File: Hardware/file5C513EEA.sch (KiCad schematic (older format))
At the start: 72 parts, among them J10 IN_2, J11 IN_3, J12 PWM_CV, J4 OUT2_CON, J5 EXT_CON, J6 CUTOFF_CV, J7 SHAPE_CV, J8 OUT1_CON, J9 IN_1, U2 MCP6002-xSN, U3 MCP6004, U4 OPA1678, U5 MCP6002-xSN

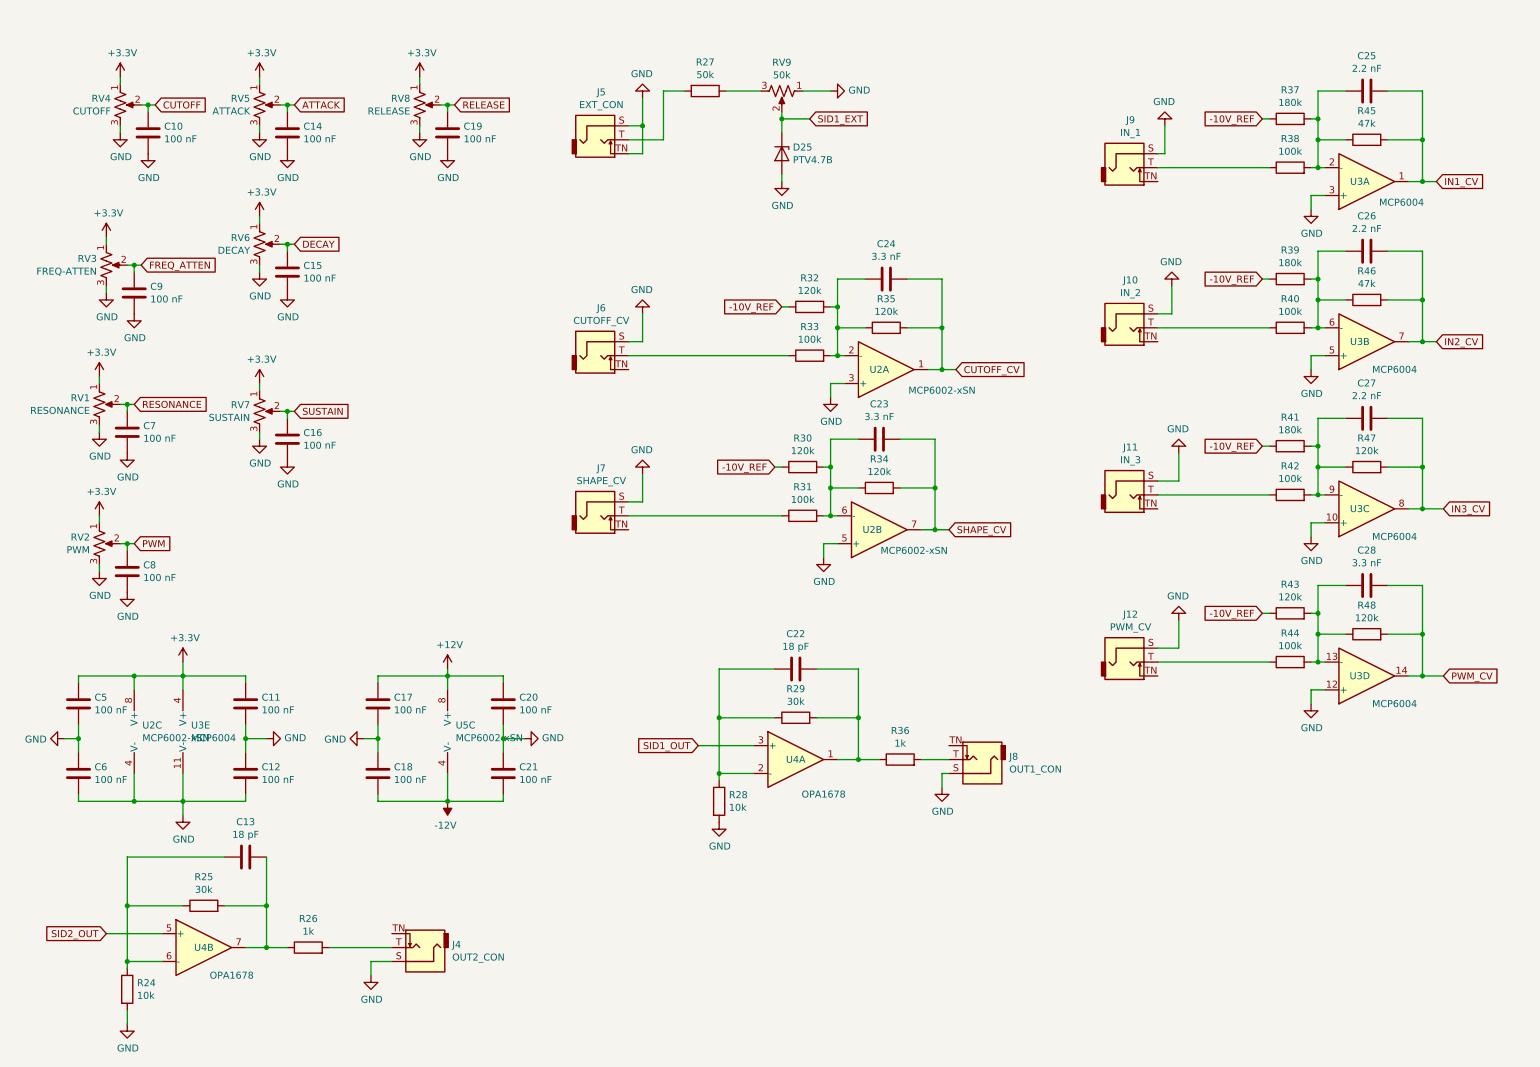
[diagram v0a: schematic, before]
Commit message: Started board layout
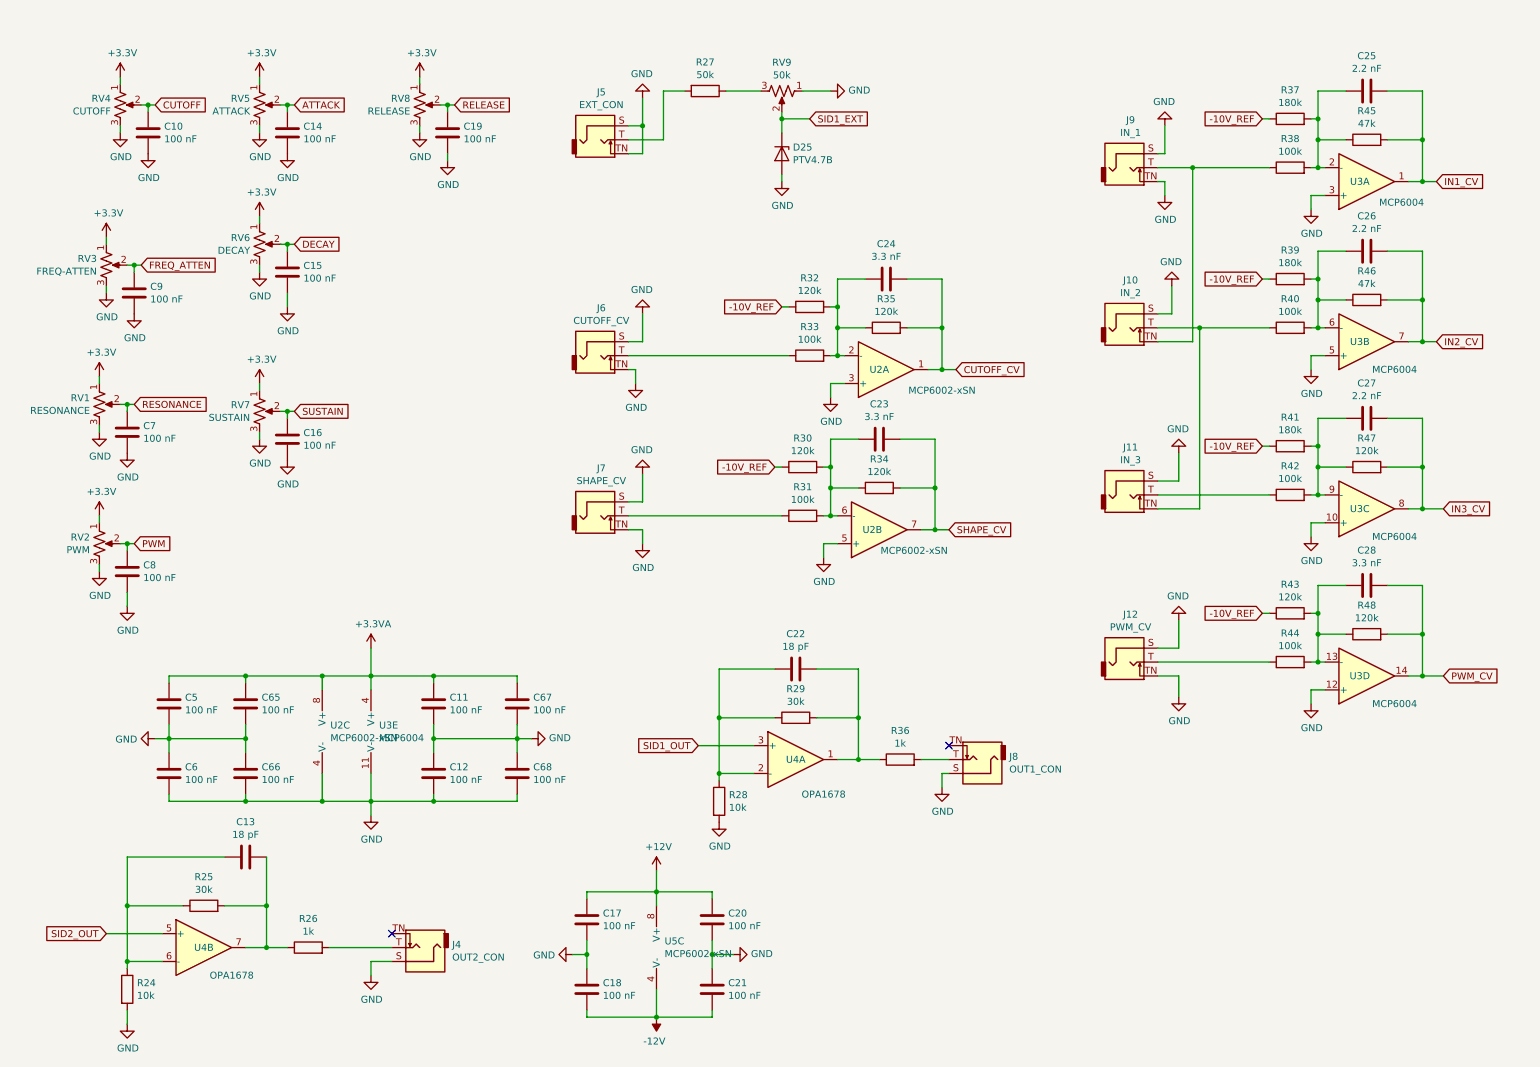
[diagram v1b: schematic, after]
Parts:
- added C65, C66, C67, C68: 100 nF, symbol Device:C
- C10, C11, C12, C13, C14, C15, C16, C17, C18, C19, C20, C21, C22, C23, C24, C25, C26, C27, C28, C5, C6, C7, C8, C9: footprint (none) -> Capacitors_SMD:C_0603
- U2, U4, U5: footprint (none) -> Housings_SOIC:SOIC-8_3.9x4.9mm_Pitch1.27mm
- U3: footprint (none) -> Housings_SSOP:TSSOP-14_4.4x5mm_Pitch0.65mm
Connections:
- net +3V3: no longer C11.1, C5.1, U2.8 (V+), U3.4 (V+)
- net GND: now also J12.TN, J6.TN, J7.TN, J9.TN, C65.2, C66.1, C66.2, C67.2, C68.1, C68.2
- net at J9.T, R38.1: now also J10.TN
- net at J10.T, R40.1: now also J11.TN
- new net +3.3VA: C11.1, C5.1, C65.1, C67.1, U2.8 (V+), U3.4 (V+)
- no-connect marks 0 -> 2
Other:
- moved on the sheet: C11, C12, C17, C18, C20, C21, C5, C6, U2C, U3E, U5C

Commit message: Fixed issues with footprints
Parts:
- C10, C11, C12, C13, C14, C15, C16, C17, C18, C19, C20, C21, C22, C23, C24, C25, C26, C27, C28, C5, C6, C7, C8, C9: footprint Capacitors_SMD:C_0603 -> Capacitor_SMD:C_0603_1608Metric
- C65, C66, C67, C68: footprint (none) -> Capacitor_SMD:C_0603_1608Metric
- U2, U4, U5: footprint Housings_SOIC:SOIC-8_3.9x4.9mm_Pitch1.27mm -> Package_SO:SOIC-8_3.9x4.9mm_P1.27mm
- U3: footprint Housings_SSOP:TSSOP-14_4.4x5mm_Pitch0.65mm -> Package_SO:TSSOP-14_4.4x5mm_P0.65mm

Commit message: Added PJ398SM model
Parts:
- J10, J11, J12, J4, J5, J6, J7, J8, J9: footprint (none) -> Connector_Audio:Jack_3.5mm_QingPu_WQP-PJ398SM_Vertical_CircularHoles
- R24, R25, R26, R27, R28, R29, R30, R31, R32, R33, R34, R35, R36, R37, R38, R39, R40, R41, R42, R43, R44, R45, R46, R47, R48: footprint (none) -> Resistor_SMD:R_0603_1608Metric
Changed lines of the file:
@@
 F 0 "J8" H 7117 5629 50  0000 R CNN
 F 1 "OUT1_CON" H 7117 5720 50  0000 R CNN
-F 2 "" H 7350 5650 50  0001 C CNN
+F 2 "Connector_Audio:Jack_3.5mm_QingPu_WQP-PJ398SM_Vertical_CircularHoles" H 7350 5650 50  0001 C CNN
 F 3 "~" H 7350 5650 50  0001 C CNN
 	1    7350 5650
@@
 F 0 "J4" H 3117 6979 50  0000 R CNN
 F 1 "OUT2_CON" H 3117 7070 50  0000 R CNN
-F 2 "" H 3350 7000 50  0001 C CNN
+F 2 "Connector_Audio:Jack_3.5mm_QingPu_WQP-PJ398SM_Vertical_CircularHoles" H 3350 7000 50  0001 C CNN
 F 3 "~" H 3350 7000 50  0001 C CNN
 	1    3350 7000
@@
 F 0 "R28" H 5570 5996 50  0000 L CNN
 F 1 "10k" H 5570 5905 50  0000 L CNN
-F 2 "" V 5430 5950 50  0001 C CNN
+F 2 "Resistor_SMD:R_0603_1608Metric" V 5430 5950 50  0001 C CNN
 F 3 "~" H 5500 5950 50  0001 C CNN
 	1    5500 5950
@@
 F 0 "R29" V 6257 5350 50  0000 C CNN
 F 1 "30k" V 6166 5350 50  0000 C CNN
-F 2 "" V 5980 5350 50  0001 C CNN
+F 2 "Resistor_SMD:R_0603_1608Metric" V 5980 5350 50  0001 C CNN
 F 3 "~" H 6050 5350 50  0001 C CNN
 	1    6050 5350
@@
 F 0 "R36" V 7007 5650 50  0000 C CNN
 F 1 "1k" V 6916 5650 50  0000 C CNN
-F 2 "" V 6730 5650 50  0001 C CNN
+F 2 "Resistor_SMD:R_0603_1608Metric" V 6730 5650 50  0001 C CNN
 F 3 "~" H 6800 5650 50  0001 C CNN
 	1    6800 5650
@@
 F 0 "R24" H 1320 7346 50  0000 L CNN
 F 1 "10k" H 1320 7255 50  0000 L CNN
-F 2 "" V 1180 7300 50  0001 C CNN
+F 2 "Resistor_SMD:R_0603_1608Metric" V 1180 7300 50  0001 C CNN
 F 3 "~" H 1250 7300 50  0001 C CNN
 	1    1250 7300
@@
 F 0 "R25" V 2007 6700 50  0000 C CNN
 F 1 "30k" V 1916 6700 50  0000 C CNN
-F 2 "" V 1730 6700 50  0001 C CNN
+F 2 "Resistor_SMD:R_0603_1608Metric" V 1730 6700 50  0001 C CNN
 F 3 "~" H 1800 6700 50  0001 C CNN
 	1    1800 6700
@@
 F 0 "R26" V 2757 7000 50  0000 C CNN
 F 1 "1k" V 2666 7000 50  0000 C CNN
-F 2 "" V 2480 7000 50  0001 C CNN
+F 2 "Resistor_SMD:R_0603_1608Metric" V 2480 7000 50  0001 C CNN
 F 3 "~" H 2550 7000 50  0001 C CNN
 	1    2550 7000
@@
 F 0 "J9" H 8454 1742 50  0000 C CNN
 F 1 "IN_1" H 8454 1651 50  0000 C CNN
-F 2 "" H 8450 1400 50  0001 C CNN
+F 2 "Connector_Audio:Jack_3.5mm_QingPu_WQP-PJ398SM_Vertical_CircularHoles" H 8450 1400 50  0001 C CNN
 F 3 "~" H 8450 1400 50  0001 C CNN
 	1    8450 1400
@@
 F 0 "R38" V 9807 1400 50  0000 C CNN
 F 1 "100k" V 9716 1400 50  0000 C CNN
-F 2 "" V 9530 1400 50  0001 C CNN
+F 2 "Resistor_SMD:R_0603_1608Metric" V 9530 1400 50  0001 C CNN
 F 3 "~" H 9600 1400 50  0001 C CNN
 	1    9600 1400
@@
 F 0 "R37" V 9807 1050 50  0000 C CNN
 F 1 "180k" V 9716 1050 50  0000 C CNN
-F 2 "" V 9530 1050 50  0001 C CNN
+F 2 "Resistor_SMD:R_0603_1608Metric" V 9530 1050 50  0001 C CNN
 F 3 "~" H 9600 1050 50  0001 C CNN
 	1    9600 1050
@@
 F 0 "R45" V 10357 1200 50  0000 C CNN
 F 1 "47k" V 10266 1200 50  0000 C CNN
-F 2 "" V 10080 1200 50  0001 C CNN
+F 2 "Resistor_SMD:R_0603_1608Metric" V 10080 1200 50  0001 C CNN
 F 3 "~" H 10150 1200 50  0001 C CNN
 	1    10150 1200
@@
 F 0 "J10" H 8454 2892 50  0000 C CNN
 F 1 "IN_2" H 8454 2801 50  0000 C CNN
-F 2 "" H 8450 2550 50  0001 C CNN
+F 2 "Connector_Audio:Jack_3.5mm_QingPu_WQP-PJ398SM_Vertical_CircularHoles" H 8450 2550 50  0001 C CNN
 F 3 "~" H 8450 2550 50  0001 C CNN
 	1    8450 2550
@@
 F 0 "R40" V 9807 2550 50  0000 C CNN
 F 1 "100k" V 9716 2550 50  0000 C CNN
-F 2 "" V 9530 2550 50  0001 C CNN
+F 2 "Resistor_SMD:R_0603_1608Metric" V 9530 2550 50  0001 C CNN
 F 3 "~" H 9600 2550 50  0001 C CNN
 	1    9600 2550
@@
 F 0 "R39" V 9807 2200 50  0000 C CNN
 F 1 "180k" V 9716 2200 50  0000 C CNN
-F 2 "" V 9530 2200 50  0001 C CNN
+F 2 "Resistor_SMD:R_0603_1608Metric" V 9530 2200 50  0001 C CNN
 F 3 "~" H 9600 2200 50  0001 C CNN
 	1    9600 2200
@@
 F 0 "R46" V 10357 2350 50  0000 C CNN
 F 1 "47k" V 10266 2350 50  0000 C CNN
-F 2 "" V 10080 2350 50  0001 C CNN
+F 2 "Resistor_SMD:R_0603_1608Metric" V 10080 2350 50  0001 C CNN
 F 3 "~" H 10150 2350 50  0001 C CNN
 	1    10150 2350
@@
 F 0 "J11" H 8454 4092 50  0000 C CNN
 F 1 "IN_3" H 8454 4001 50  0000 C CNN
-F 2 "" H 8450 3750 50  0001 C CNN
+F 2 "Connector_Audio:Jack_3.5mm_QingPu_WQP-PJ398SM_Vertical_CircularHoles" H 8450 3750 50  0001 C CNN
 F 3 "~" H 8450 3750 50  0001 C CNN
 	1    8450 3750
@@
 F 0 "R42" V 9807 3750 50  0000 C CNN
 F 1 "100k" V 9716 3750 50  0000 C CNN
-F 2 "" V 9530 3750 50  0001 C CNN
+F 2 "Resistor_SMD:R_0603_1608Metric" V 9530 3750 50  0001 C CNN
 F 3 "~" H 9600 3750 50  0001 C CNN
 	1    9600 3750
@@
 F 0 "R41" V 9807 3400 50  0000 C CNN
 F 1 "180k" V 9716 3400 50  0000 C CNN
-F 2 "" V 9530 3400 50  0001 C CNN
+F 2 "Resistor_SMD:R_0603_1608Metric" V 9530 3400 50  0001 C CNN
 F 3 "~" H 9600 3400 50  0001 C CNN
 	1    9600 3400
@@
 F 0 "R47" V 10357 3550 50  0000 C CNN
 F 1 "120k" V 10266 3550 50  0000 C CNN
-F 2 "" V 10080 3550 50  0001 C CNN
+F 2 "Resistor_SMD:R_0603_1608Metric" V 10080 3550 50  0001 C CNN
 F 3 "~" H 10150 3550 50  0001 C CNN
 	1    10150 3550
@@
 F 0 "J12" H 8454 5292 50  0000 C CNN
 F 1 "PWM_CV" H 8454 5201 50  0000 C CNN
-F 2 "" H 8450 4950 50  0001 C CNN
+F 2 "Connector_Audio:Jack_3.5mm_QingPu_WQP-PJ398SM_Vertical_CircularHoles" H 8450 4950 50  0001 C CNN
 F 3 "~" H 8450 4950 50  0001 C CNN
 	1    8450 4950
@@
 F 0 "R44" V 9807 4950 50  0000 C CNN
 F 1 "100k" V 9716 4950 50  0000 C CNN
-F 2 "" V 9530 4950 50  0001 C CNN
+F 2 "Resistor_SMD:R_0603_1608Metric" V 9530 4950 50  0001 C CNN
 F 3 "~" H 9600 4950 50  0001 C CNN
 	1    9600 4950
@@
 F 0 "R43" V 9807 4600 50  0000 C CNN
 F 1 "120k" V 9716 4600 50  0000 C CNN
-F 2 "" V 9530 4600 50  0001 C CNN
+F 2 "Resistor_SMD:R_0603_1608Metric" V 9530 4600 50  0001 C CNN
 F 3 "~" H 9600 4600 50  0001 C CNN
 	1    9600 4600
@@
 F 0 "R48" V 10357 4750 50  0000 C CNN
 F 1 "120k" V 10266 4750 50  0000 C CNN
-F 2 "" V 10080 4750 50  0001 C CNN
+F 2 "Resistor_SMD:R_0603_1608Metric" V 10080 4750 50  0001 C CNN
 F 3 "~" H 10150 4750 50  0001 C CNN
 	1    10150 4750
@@
 F 0 "J5" H 4654 1542 50  0000 C CNN
 F 1 "EXT_CON" H 4654 1451 50  0000 C CNN
-F 2 "" H 4650 1200 50  0001 C CNN
+F 2 "Connector_Audio:Jack_3.5mm_QingPu_WQP-PJ398SM_Vertical_CircularHoles" H 4650 1200 50  0001 C CNN
 F 3 "~" H 4650 1200 50  0001 C CNN
 	1    4650 1200
@@
 F 0 "J6" H 4654 3092 50  0000 C CNN
 F 1 "CUTOFF_CV" H 4654 3001 50  0000 C CNN
-F 2 "" H 4650 2750 50  0001 C CNN
+F 2 "Connector_Audio:Jack_3.5mm_QingPu_WQP-PJ398SM_Vertical_CircularHoles" H 4650 2750 50  0001 C CNN
 F 3 "~" H 4650 2750 50  0001 C CNN
 	1    4650 2750
@@
 F 0 "J7" H 4654 4242 50  0000 C CNN
 F 1 "SHAPE_CV" H 4654 4151 50  0000 C CNN
-F 2 "" H 4650 3900 50  0001 C CNN
+F 2 "Connector_Audio:Jack_3.5mm_QingPu_WQP-PJ398SM_Vertical_CircularHoles" H 4650 3900 50  0001 C CNN
 F 3 "~" H 4650 3900 50  0001 C CNN
 	1    4650 3900
@@
 F 0 "R27" V 5193 850 50  0000 C CNN
 F 1 "50k" V 5284 850 50  0000 C CNN
-F 2 "" V 5330 850 50  0001 C CNN
+F 2 "Resistor_SMD:R_0603_1608Metric" V 5330 850 50  0001 C CNN
 F 3 "~" H 5400 850 50  0001 C CNN
 	1    5400 850
@@
 F 0 "R33" V 6357 2750 50  0000 C CNN
 F 1 "100k" V 6266 2750 50  0000 C CNN
-F 2 "" V 6080 2750 50  0001 C CNN
+F 2 "Resistor_SMD:R_0603_1608Metric" V 6080 2750 50  0001 C CNN
 F 3 "~" H 6150 2750 50  0001 C CNN
 	1    6150 2750
@@
 F 0 "R32" V 6357 2400 50  0000 C CNN
 F 1 "120k" V 6266 2400 50  0000 C CNN
-F 2 "" V 6080 2400 50  0001 C CNN
+F 2 "Resistor_SMD:R_0603_1608Metric" V 6080 2400 50  0001 C CNN
 F 3 "~" H 6150 2400 50  0001 C CNN
 	1    6150 2400
@@
 F 0 "R35" V 6907 2550 50  0000 C CNN
 F 1 "120k" V 6816 2550 50  0000 C CNN
-F 2 "" V 6630 2550 50  0001 C CNN
+F 2 "Resistor_SMD:R_0603_1608Metric" V 6630 2550 50  0001 C CNN
 F 3 "~" H 6700 2550 50  0001 C CNN
 	1    6700 2550
@@
 F 0 "R31" V 6307 3900 50  0000 C CNN
 F 1 "100k" V 6216 3900 50  0000 C CNN
-F 2 "" V 6030 3900 50  0001 C CNN
+F 2 "Resistor_SMD:R_0603_1608Metric" V 6030 3900 50  0001 C CNN
 F 3 "~" H 6100 3900 50  0001 C CNN
 	1    6100 3900
@@
 F 0 "R30" V 6307 3550 50  0000 C CNN
 F 1 "120k" V 6216 3550 50  0000 C CNN
-F 2 "" V 6030 3550 50  0001 C CNN
+F 2 "Resistor_SMD:R_0603_1608Metric" V 6030 3550 50  0001 C CNN
 F 3 "~" H 6100 3550 50  0001 C CNN
 	1    6100 3550
@@
 F 0 "R34" V 6857 3700 50  0000 C CNN
 F 1 "120k" V 6766 3700 50  0000 C CNN
-F 2 "" V 6580 3700 50  0001 C CNN
+F 2 "Resistor_SMD:R_0603_1608Metric" V 6580 3700 50  0001 C CNN
 F 3 "~" H 6650 3700 50  0001 C CNN
 	1    6650 3700

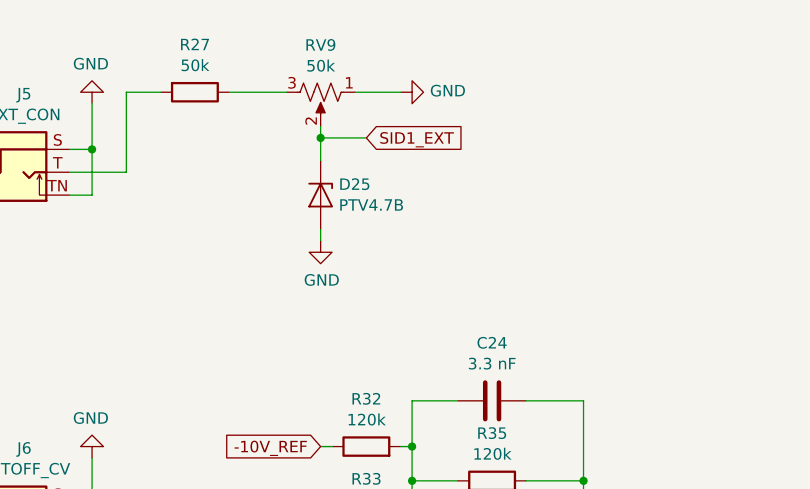
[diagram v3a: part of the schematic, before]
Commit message: Finished assigning footprints
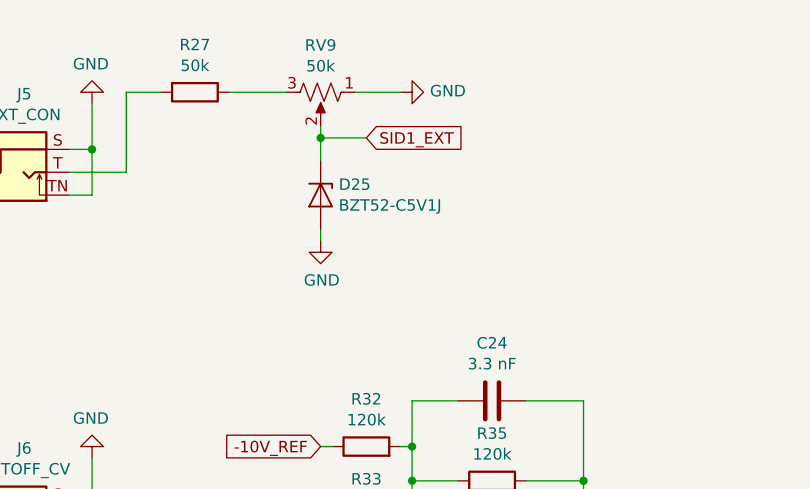
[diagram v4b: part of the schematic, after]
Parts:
- D25: value PTV4.7B -> BZT52-C5V1J; footprint (none) -> Diode_SMD:D_SOD-123
- RV1, RV2, RV3, RV4, RV9: footprint (none) -> Potentiometer_THT:Potentiometer_Bourns_PTV09A-1_Single_Vertical
- RV5, RV6, RV7, RV8: footprint (none) -> Potentiometer_THT:Potentiometer_Bourns_PTA2043_Single_Slide
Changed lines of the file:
@@
 F 0 "RV4" H 1132 996 50  0000 R CNN
 F 1 "CUTOFF" H 1132 905 50  0000 R CNN
-F 2 "" H 1200 950 50  0001 C CNN
+F 2 "Potentiometer_THT:Potentiometer_Bourns_PTV09A-1_Single_Vertical" H 1200 950 50  0001 C CNN
 F 3 "~" H 1200 950 50  0001 C CNN
 	1    1200 950
@@
 F 0 "RV1" H 982 3146 50  0000 R CNN
 F 1 "RESONANCE" H 982 3055 50  0000 R CNN
-F 2 "" H 1050 3100 50  0001 C CNN
+F 2 "Potentiometer_THT:Potentiometer_Bourns_PTV09A-1_Single_Vertical" H 1050 3100 50  0001 C CNN
 F 3 "~" H 1050 3100 50  0001 C CNN
 	1    1050 3100
@@
 F 0 "RV2" H 982 4146 50  0000 R CNN
 F 1 "PWM" H 982 4055 50  0000 R CNN
-F 2 "" H 1050 4100 50  0001 C CNN
+F 2 "Potentiometer_THT:Potentiometer_Bourns_PTV09A-1_Single_Vertical" H 1050 4100 50  0001 C CNN
 F 3 "~" H 1050 4100 50  0001 C CNN
 	1    1050 4100
@@
 F 0 "RV5" H 2132 996 50  0000 R CNN
 F 1 "ATTACK" H 2132 905 50  0000 R CNN
-F 2 "" H 2200 950 50  0001 C CNN
+F 2 "Potentiometer_THT:Potentiometer_Bourns_PTA2043_Single_Slide" H 2200 950 50  0001 C CNN
 F 3 "~" H 2200 950 50  0001 C CNN
 	1    2200 950
@@
 F 0 "RV6" H 2132 1996 50  0000 R CNN
 F 1 "DECAY" H 2132 1905 50  0000 R CNN
-F 2 "" H 2200 1950 50  0001 C CNN
+F 2 "Potentiometer_THT:Potentiometer_Bourns_PTA2043_Single_Slide" H 2200 1950 50  0001 C CNN
 F 3 "~" H 2200 1950 50  0001 C CNN
 	1    2200 1950
@@
 F 0 "RV7" H 2132 3196 50  0000 R CNN
 F 1 "SUSTAIN" H 2132 3105 50  0000 R CNN
-F 2 "" H 2200 3150 50  0001 C CNN
+F 2 "Potentiometer_THT:Potentiometer_Bourns_PTA2043_Single_Slide" H 2200 3150 50  0001 C CNN
 F 3 "~" H 2200 3150 50  0001 C CNN
 	1    2200 3150
@@
 F 0 "RV8" H 3282 996 50  0000 R CNN
 F 1 "RELEASE" H 3282 905 50  0000 R CNN
-F 2 "" H 3350 950 50  0001 C CNN
+F 2 "Potentiometer_THT:Potentiometer_Bourns_PTA2043_Single_Slide" H 3350 950 50  0001 C CNN
 F 3 "~" H 3350 950 50  0001 C CNN
 	1    3350 950
@@
 F 0 "RV3" H 1032 2146 50  0000 R CNN
 F 1 "FREQ-ATTEN" H 1032 2055 50  0000 R CNN
-F 2 "" H 1100 2100 50  0001 C CNN
+F 2 "Potentiometer_THT:Potentiometer_Bourns_PTV09A-1_Single_Vertical" H 1100 2100 50  0001 C CNN
 F 3 "~" H 1100 2100 50  0001 C CNN
 	1    1100 2100
@@
 F 0 "RV9" V 5745 850 50  0000 C CNN
 F 1 "50k" V 5836 850 50  0000 C CNN
-F 2 "" H 5950 850 50  0001 C CNN
+F 2 "Potentiometer_THT:Potentiometer_Bourns_PTV09A-1_Single_Vertical" H 5950 850 50  0001 C CNN
 F 3 "~" H 5950 850 50  0001 C CNN
 	1    5950 850
@@
 Wire Wire Line
 	6100 850  6300 850
-$Comp
-L Device:D_Zener D?
-U 1 1 5C5D98C1
-P 5950 1300
-AR Path="/5BFD63E3/5C5D98C1" Ref="D?"  Part="1"
-AR Path="/5BFD63E3/5C513EEB/5C5D98C1" Ref="D25"  Part="1"
-F 0 "D25" V 5904 1379 50  0000 L CNN
-F 1 "PTV4.7B" V 5995 1379 50  0000 L CNN
-F 2 "" H 5950 1300 50  0001 C CNN
-F 3 "~" H 5950 1300 50  0001 C CNN
-	1    5950 1300
-	0    1    1    0
-$EndComp
 Wire Wire Line
 	5950 1150 5950 1050
@@
 Wire Wire Line
 	3450 5500 3450 5600
+$Comp
+L Device:D_Zener D?
+U 1 1 5C5D98C1
+P 5950 1300
+AR Path="/5BFD63E3/5C5D98C1" Ref="D?"  Part="1"
+AR Path="/5BFD63E3/5C513EEB/5C5D98C1" Ref="D25"  Part="1"
+F 0 "D25" V 5904 1379 50  0000 L CNN
+F 1 "BZT52-C5V1J" V 5995 1379 50  0000 L CNN
+F 2 "Diode_SMD:D_SOD-123" H 5950 1300 50  0001 C CNN
+F 3 "~" H 5950 1300 50  0001 C CNN
+	1    5950 1300
+	0    1    1    0
+$EndComp
 $EndSCHEMATC
